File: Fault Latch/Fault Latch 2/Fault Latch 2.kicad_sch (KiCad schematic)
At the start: 51 parts, among them J101 Inputs, K103 Fujitsu_FTR-LYAA005x, K104 Fujitsu_FTR-LYAA005x, K105 Fujitsu_FTR-LYAA005x, Q1 PMOS, Q101 NMOS, Q104 NMOS, Q108 NMOS, Q109 NMOS, Q110 NMOS, Q2 PMOS, SW1 SW_Omron_B3FS, SW2 SW_Omron_B3FS, SW3 SW_Omron_B3FS, U103 74AHC1G00, U104 74LS279, U105 SFH617A-1, U106 74AHC1G00, U108 SFH617A-1, U109 74AHC1G00, U111 SFH617A-1

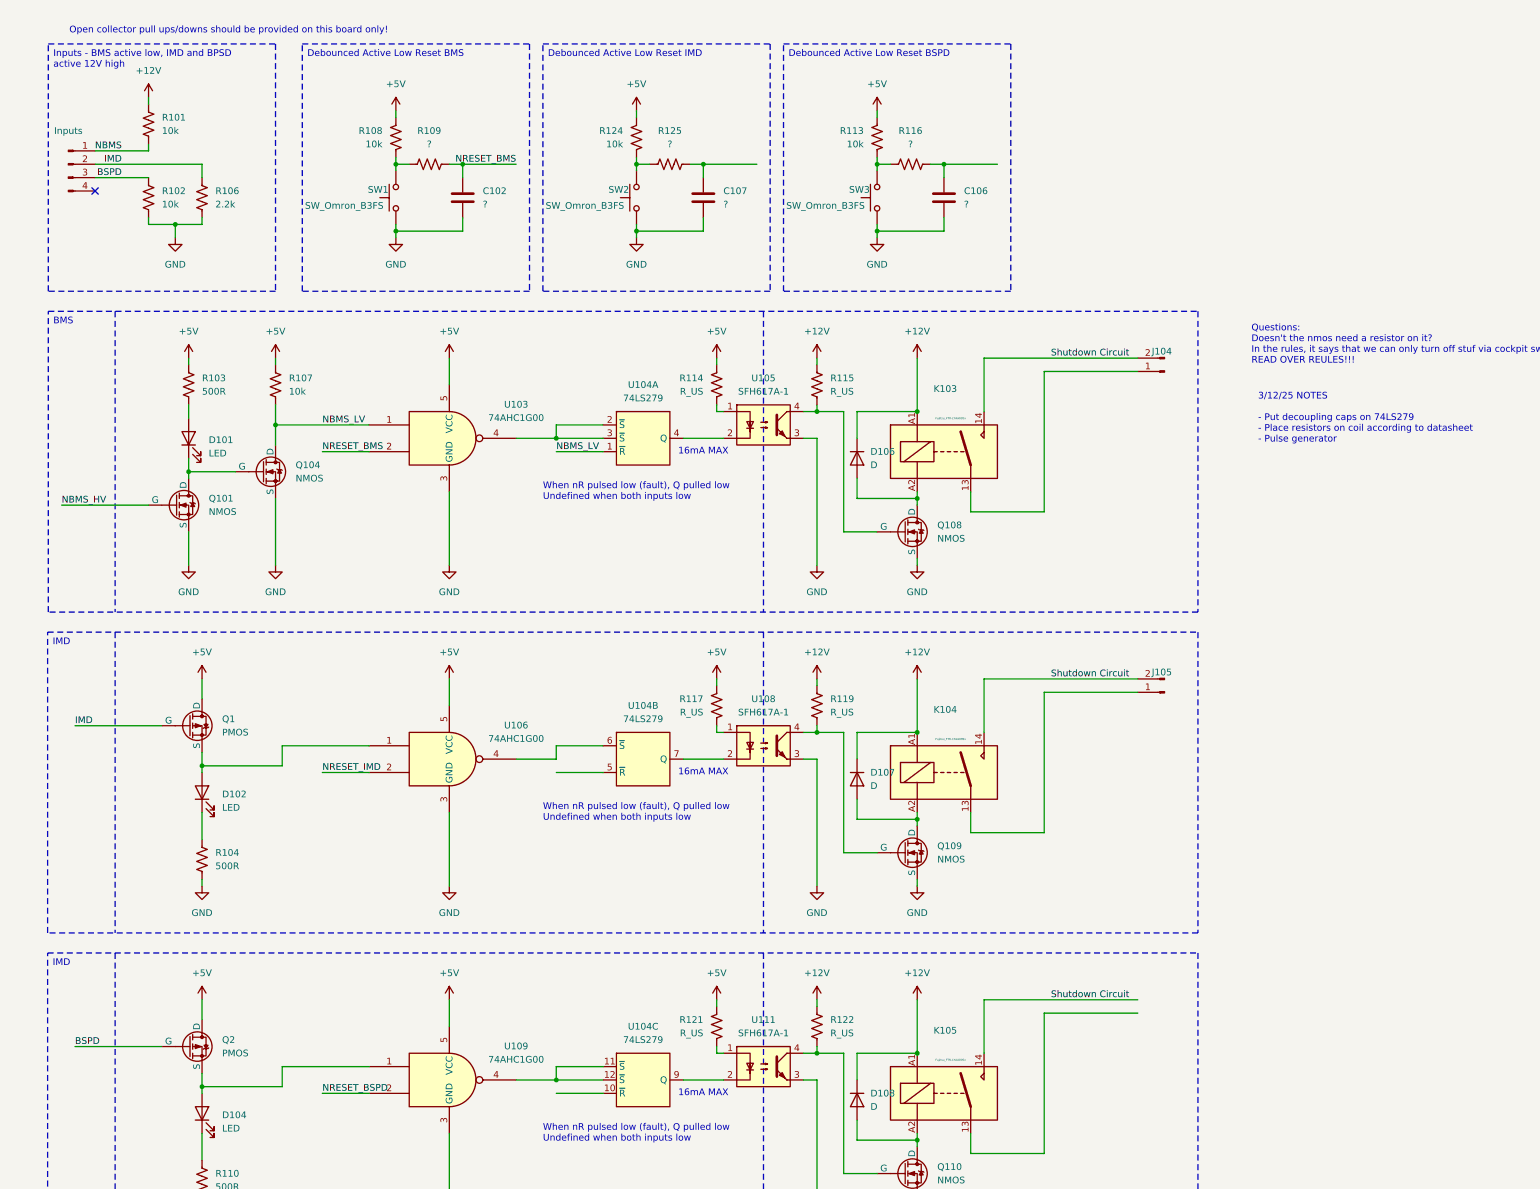
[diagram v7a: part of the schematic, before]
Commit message: Added the pulse generators for the buttons
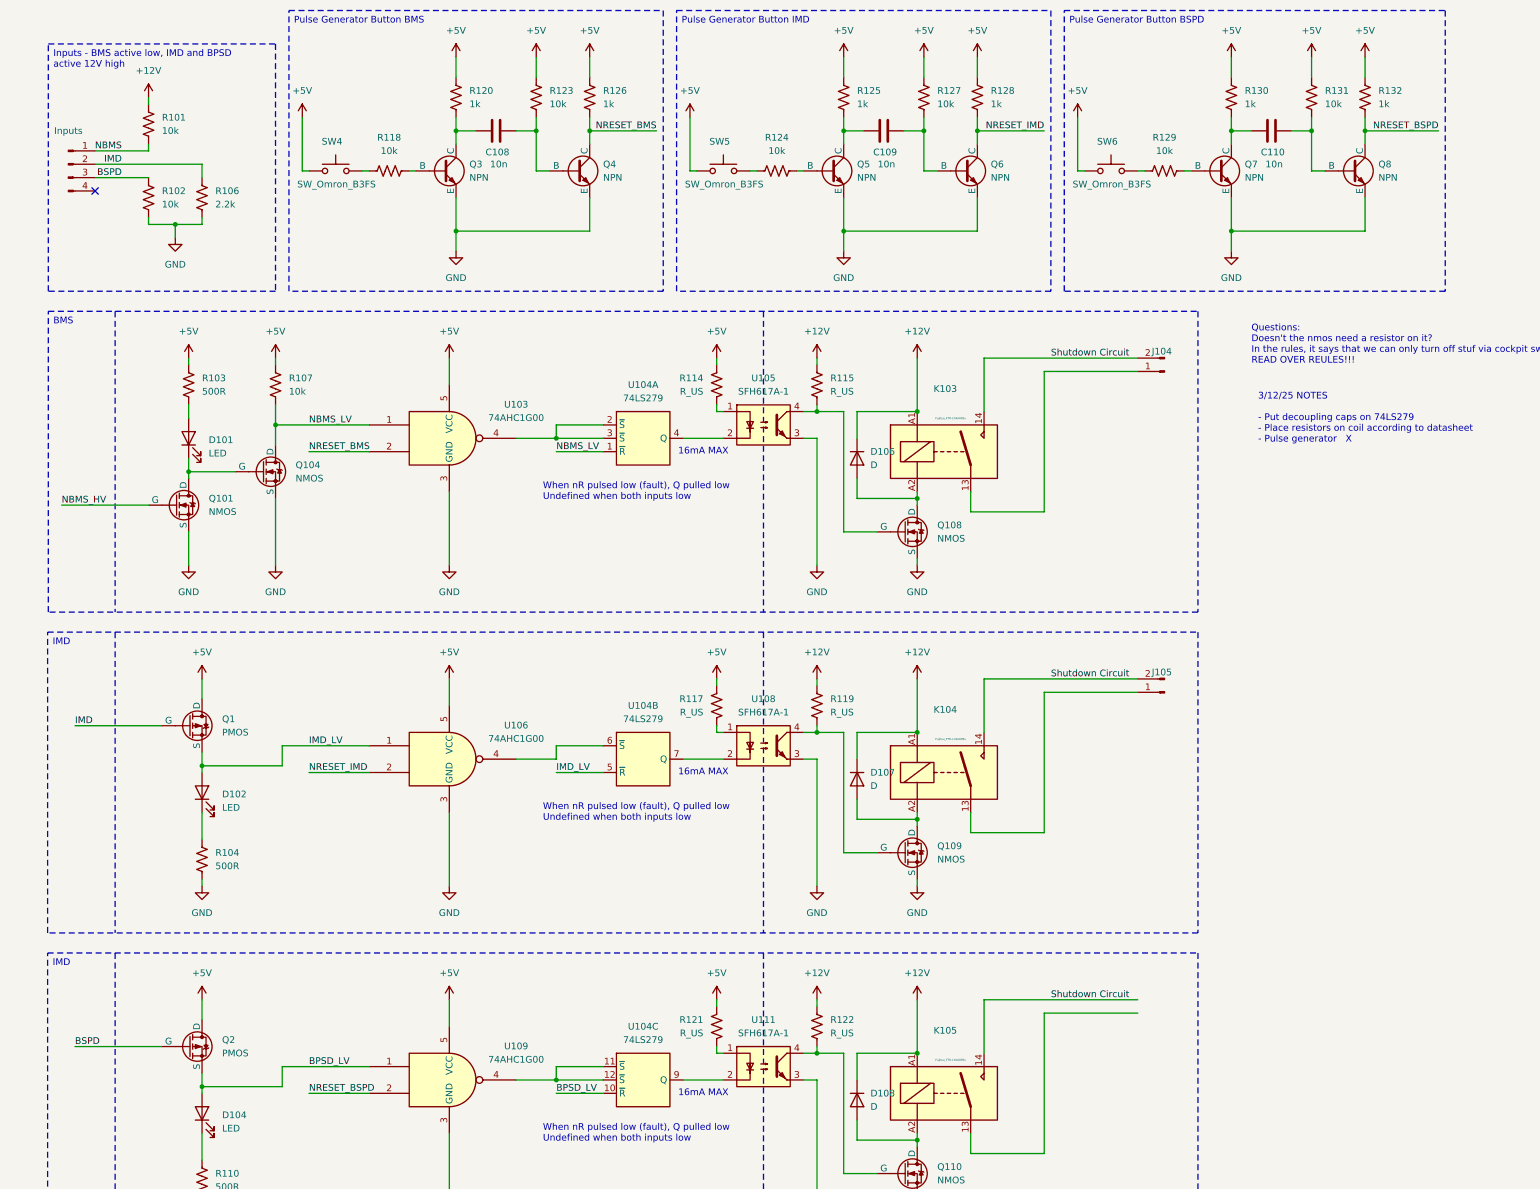
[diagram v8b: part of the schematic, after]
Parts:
- removed C102, C106, C107: ?, symbol Device:C
- removed R108, R113: 10k, symbol Device:R_US
- removed R109, R116: ?, symbol Device:R_US
- removed SW1, SW2, SW3: SW_Omron_B3FS, Button_Switch_SMD:SW_SPST_Omron_B3FS-100xP, symbol Switch:SW_Omron_B3FS
- added C108, C109, C110: 10n, symbol Device:C
- added Q3, Q4, Q5, Q6, Q7, Q8: NPN, symbol Simulation_SPICE:NPN
- added R118, R123, R127, R129, R131: 10k, symbol Device:R_US
- added R120, R126, R128, R130, R132: 1k, symbol Device:R_US
- added SW4, SW5, SW6: SW_Omron_B3FS, Button_Switch_SMD:SW_SPST_Omron_B3FS-100xP, symbol Switch:SW_Omron_B3FS
- R125: value ? -> 1k
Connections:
- net +5V: now also R125.1, R120.1, R123.1, R126.1, R127.1, R128.1, R130.1, R131.1, R132.1, SW4.1, SW5.1, SW6.1; no longer R124.2
- net GND: now also Q3.3 (E), Q4.3 (E), Q5.3 (E), Q6.3 (E), Q7.3 (E), Q8.3 (E)
- net NRESET_BMS: now also Q4.1 (C), R126.2
- net NRESET_BSPD: now also Q8.1 (C), R132.2
- net NRESET_IMD: now also Q6.1 (C), R128.2
- net BPSD_LV: now reaches U104.10 (~{R})
- net BPSD_LV: now also D104.2 (A), Q2.3 (S), U109.1
- net IMD_LV: now reaches D102.2 (A), Q1.3 (S), U106.1
- net IMD_LV: now also U104.5 (~{R})
- net at R125.2: now also C109.1, Q5.1 (C); no longer R124.1
- new net: Q5.2 (B), R124.1
- new net: C108.1, Q3.1 (C), R120.2
- new net: Q3.2 (B), R118.1
- new net: C110.1, Q7.1 (C), R130.2
- new net: Q7.2 (B), R129.1
- new net: R124.2, SW5.2
- new net: C110.2, Q8.2 (B), R131.2
- new net: C109.2, Q6.2 (B), R127.2
- new net: C108.2, Q4.2 (B), R123.2
- new net: R118.2, SW4.2
- new net: R129.2, SW6.2
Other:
- note added: "3/12/25 NOTES - Put decoupling caps on 74LS279 - Place resistors on coil according to datasheet - Pulse generator X"
- note removed: "3/12/25 NOTES - Put decoupling caps on 74LS279 - Place resistors on coil according to datasheet - Pulse generator"
- note removed: "Open collector pull ups/downs should be provided on this board only!"
